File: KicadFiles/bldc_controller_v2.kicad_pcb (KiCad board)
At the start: 2 copper layers, 60 x 89 mm, 181 parts, among them J1 Conn_01x05_Male, J10 Conn_01x02_Female, J11 Conn_01x02_Female, J12 Conn_01x02_Female, J13 Conn_01x02_Female, J14 Conn_01x02_Female, J15 Conn_01x04_Male, J2 Conn_01x03_Male, J3 Conn_01x03_Male, J4 1935174, J5 Conn_01x02_Female, J9 Conn_01x02_Female, Q1 DMN65D8L-7, Q10 IRLB8721PBF, Q11 IRLB8721PBF, Q2 DMN65D8L-7, Q3 DMN65D8L-7, Q4 DMN65D8L-7, Q5 IRF4905, Q6 IRLB8721PBF, Q7 IRLB8721PBF, Q8 IRLB8721PBF, Q9 IRLB8721PBF, SW2 D6C40 F1 LFS, SW3 1301.9314, SW4 1301.9314, SW5 SW_Push_DPDT, U1 ATmega328P-PU, U2 uA7810, U3 LM7805_TO220, U4 MCP601-xP, U5 LM339, U6 IRS2004, U7 IRS2004, U8 IRS2004, U9 HCPL-181-00DE, Y1 9B-16.000MBBK-B

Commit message: Need to Update MCU Signals
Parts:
- C14, C22, C24, C28, C29, C32, D12, D13, D16, R10, R12, R13, R20, R22, R26, R33, R34, R35, R36, R37, R38, R39, R44, R45: moved to B.Cu
- moved D12 133.2 mm to (156.0, 140.2), turned to 270 degrees
- moved R10 124.8 mm to (163.2, 140.2), turned to 90 degrees
- moved D13 123.0 mm to (128.4, 144.0), turned to 270 degrees
- moved R20 122.7 mm to (140.5, 144.0), turned to 90 degrees
- moved R12 119.6 mm to (158.4, 140.2), turned to 270 degrees
- moved R5 114.8 mm to (70.2, 121.2)
- moved C14 114.2 mm to (160.8, 140.2), turned to 90 degrees
- moved D16 108.6 mm to (135.0, 104.5), turned to 180 degrees
- moved R26 108.3 mm to (142.8, 144.0), turned to 270 degrees
- moved R51 108.3 mm to (178.0, 124.4)
- moved C22 107.4 mm to (138.2, 144.0), turned to 90 degrees
- moved R49 103.6 mm to (167.8, 124.0)
- moved C24 101.9 mm to (133.0, 144.0), turned to 90 degrees
- moved R50 99.9 mm to (175.6, 116.8)
- moved R46 97.6 mm to (168.4, 119.0)
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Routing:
- net Net-(R37-Pad2): track 6.14 -> 14.6 mm, vias 0 -> 1
- net GNDD: track 0.00 -> 2.79 mm, vias 0 -> 1
- net /GATE_A_HI: track 0.00 -> 2.77 mm
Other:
- board size 60 x 89 mm -> 51.5 x 89 mm
- copper layers 2 -> 4

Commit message: Ready to Route
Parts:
- removed C13: 1uF, Capacitor_SMD:C_0805_2012Metric_Pad1.15x1.40mm_HandSolder
- removed D11: BAT54HT1G, Diode_SMD:D_SOD-323_HandSoldering
- removed D3: LTST-C171KRKT, LED_SMD:LED_0805_2012Metric_Pad1.15x1.40mm_HandSolder
- removed Q1, Q4: DMN65D8L-7, Package_TO_SOT_SMD:SOT-23
- removed R11: 100K, Resistor_SMD:R_0805_2012Metric_Pad1.15x1.40mm_HandSolder
- removed R18, R9: 10K, Resistor_SMD:R_0805_2012Metric_Pad1.15x1.40mm_HandSolder
- removed R2: 300, Resistor_SMD:R_0805_2012Metric_Pad1.15x1.40mm_HandSolder
- C15, C16, C23, C26, C36, C4, C6, C8, R15, R16, R17, R27, R28, R29, R30, R46, R47, R48, R52: moved to B.Cu
- moved J14 126.5 mm to (159.8, 135.2), turned to 90 degrees
- moved J11 124.3 mm to (156.0, 135.2), turned to 270 degrees
- moved J9 123.3 mm to (162.2, 128.0), turned to 270 degrees
- moved J10 123.0 mm to (147.2, 135.2), turned to 90 degrees
- moved J12 122.7 mm to (162.2, 131.5), turned to 270 degrees
- moved R3 121.8 mm to (156.0, 65.0)
- moved D6 116.1 mm to (152.0, 71.8), turned to 180 degrees
- moved J13 115.0 mm to (143.5, 135.2), turned to 270 degrees
- moved R6 112.0 mm to (156.0, 69.5)
- moved D1 110.6 mm to (152.0, 62.8), turned to 180 degrees
- moved D10 108.4 mm to (152.0, 74.0), turned to 180 degrees
- moved Q2 106.0 mm to (159.8, 71.0), turned to 180 degrees
- moved R7 103.8 mm to (156.0, 74.0)
- moved D7 103.1 mm to (152.0, 67.2), turned to 180 degrees
- moved C36 102.0 mm to (143.1, 128.0), turned to 90 degrees
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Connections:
- U1 pad 11: /nESTOP -> /MCU_C_EN
- U1 pad 12: /BEMF_A -> /MCU_C_SIG
- U1 pad 13: /BEMF_C -> /MCU_B_EN
- U1 pad 14: /BEMF_B -> /MCU_A_EN
- U1 pad 15: /MCU_C_SIG -> /MCU_A_SIG
- U1 pad 17: /MCU_A_SIG -> /EFUSE_EN
- U1 pad 18: /MCU_C_EN -> /AUX_OUT
- U1 pad 19: /MCU_B_EN -> /nESTOP
- U1 pad 23: /MCU_A_EN -> /ANALOG_IN
- U1 pad 24: /EFUSE_EN -> /AUX_IN
- U1 pad 25: /ANALOG_IN -> /I_SENSE
- U1 pad 26: /I_SENSE -> /BEMF_A
- U1 pad 4: /nI_TRIG -> /BEMF_C
- U1 pad 5: /AUX_IN -> /nI_TRIG
- U1 pad 6: /AUX_OUT -> /BEMF_B
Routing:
- net /EFUSE_GATE: track 0.00 -> 6.73 mm
- net /V_MOTOR: track 0.00 -> 4.85 mm
- net GNDD: track 2.79 -> 0.15 mm, vias 1 -> 0

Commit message: Began Routing
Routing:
- added copper zone on B.Cu, net +12V
- added copper zone on F.Cu, net +12V
- added copper zone on B.Cu, net +BATT
- added copper zone on F.Cu, net +BATT
- added copper zone on B.Cu, net /I_RAW
- added copper zone on B.Cu, net /V_MOTOR
- added copper zone on F.Cu, net /V_MOTOR
- added copper zone on B.Cu, net Net-(F1-Pad1)
- added copper zone on F.Cu, net Net-(F1-Pad1)
- added copper zone on F.Cu, net VBUS
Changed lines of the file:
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@@
   )
   (setup
-    (last_trace_width 0.762)
+    (last_trace_width 1.905)
     (user_trace_width 0.254)
     (user_trace_width 0.508)
     (user_trace_width 0.762)
     (user_trace_width 1.27)
+    (user_trace_width 1.905)
     (trace_clearance 0.2)
     (zone_clearance 0.508)
-    (zone_45_only no)
+    (zone_45_only yes)
     (trace_min 0.2)
     (via_size 0.8)
@@
   (segment (start 138.79 84.75) (end 138.75 84.79) (width 0.762) (layer In1.Cu) (net 67))
   (segment (start 146 84.75) (end 138.79 84.75) (width 0.762) (layer In1.Cu) (net 67))
+  (zone (net 2) (net_name +BATT) (layer F.Cu) (hatch edge 0.508)
+    (connect_pads (clearance 0.508))
+    (min_thickness 0.254)
+    (fill yes (arc_segments 32) (thermal_gap 0.508) (thermal_bridge_width 0.508))
+    (polygon
+      (pts
+        (xy 113.25 71) (xy 121.75 71) (xy 121.75 61.25) (xy 115.5 61.25) (xy 113.25 63.5)
+      )
+    )
+  )
+  (zone (net 2) (net_name +BATT) (layer B.Cu) (hatch edge 0.508)
+    (connect_pads (clearance 0.508))
+    (min_thickness 0.254)
+    (fill yes (arc_segments 32) (thermal_gap 0.508) (thermal_bridge_width 0.508))
+    (polygon
+      (pts
+        (xy 113.25 71) (xy 121.75 71) (xy 121.75 61.25) (xy 115.5 61.25) (xy 113.25 63.5)
+      )
+    )
+  )
+  (zone (net 32) (net_name "Net-(F1-Pad1)") (layer B.Cu) (hatch edge 0.508)
+    (connect_pads (clearance 0.508))
+    (min_thickness 0.254)
+    (fill yes (arc_segments 32) (thermal_gap 0.508) (thermal_bridge_width 0.508))
+    (polygon
+      (pts
+        (xy 122.75 71) (xy 128 71) (xy 128 61.25) (xy 122.75 61.25)
+      )
+    )
+  )
+  (zone (net 32) (net_name "Net-(F1-Pad1)") (layer F.Cu) (hatch edge 0.508)
+    (connect_pads (clearance 0.508))
+    (min_thickness 0.254)
+    (fill yes (arc_segments 32) (thermal_gap 0.508) (thermal_bridge_width 0.508))
+    (polygon
+      (pts
+        (xy 122.75 71) (xy 128 71) (xy 128 61.25) (xy 122.75 61.25)
+      )
+    )
+  )
+  (zone (net 7) (net_name +12V) (layer F.Cu) (hatch edge 0.508)
+    (connect_pads (clearance 0.508))
+    (min_thickness 0.254)
+    (fill yes (arc_segments 32) (thermal_gap 0.508) (thermal_bridge_width 0.508))
+    (polygon
+      (pts
+        (xy 130 61.25) (xy 130 71) (xy 136 71) (xy 136 61.25)
+      )
+    )
+  )
+  (zone (net 7) (net_name +12V) (layer B.Cu) (hatch edge 0.508)
+    (connect_pads (clearance 0.508))
+    (min_thickness 0.254)
+    (fill yes (arc_segments 32) (thermal_gap 0.508) (thermal_bridge_width 0.508))
+    (polygon
+      (pts
+        (xy 130 61.25) (xy 130 71) (xy 136 71) (xy 136 61.25)
+      )
+    )
+  )
+  (zone (net 12) (net_name /V_MOTOR) (layer F.Cu) (hatch edge 0.508)
+    (connect_pads (clearance 0.508))
+    (min_thickness 0.254)
+    (fill yes (arc_segments 32) (thermal_gap 0.508) (thermal_bridge_width 0.508))
+    (polygon
+      (pts
+        (xy 136.5 71) (xy 136.5 61.25) (xy 142 61.25) (xy 142 71)
+      )
+    )
+  )
+  (zone (net 12) (net_name /V_MOTOR) (layer B.Cu) (hatch edge 0.508)
+    (connect_pads (clearance 0.508))
+    (min_thickness 0.254)
+    (fill yes (arc_segments 32) (thermal_gap 0.508) (thermal_bridge_width 0.508))
+    (polygon
+      (pts
+        (xy 136.5 71) (xy 136.5 61.25) (xy 142 61.25) (xy 142 71)
+      )
+    )
+  )
+  (zone (net 3) (net_name VBUS) (layer F.Cu) (hatch edge 0.508)
+    (connect_pads (clearance 0.508))
+    (min_thickness 0.254)
+    (fill yes (arc_segments 32) (thermal_gap 0.508) (thermal_bridge_width 0.508))
+    (polygon
+      (pts
+        (xy 142.5 68) (xy 142.5 71.75) (xy 140 71.75) (xy 140 110.25) (xy 149.25 110.25)
+        (xy 149.25 61.25) (xy 142.5 61.25) (xy 142.5 71.75) (xy 142.5 68.25)
+      )
+    )
+  )
+  (zone (net 45) (net_name /I_RAW) (layer B.Cu) (hatch edge 0.508)
+    (connect_pads (clearance 0.508))
+    (min_thickness 0.254)
+    (fill yes (arc_segments 32) (thermal_gap 0.508) (thermal_bridge_width 0.508))
+    (polygon
+      (pts
+        (xy 135.75 75) (xy 135.75 79.5) (xy 140 79.5) (xy 140 110.25) (xy 147 110.25)
+        (xy 147 103.75) (xy 157 103.75) (xy 157 97.75) (xy 147 97.75) (xy 147 92.5)
+        (xy 157 92.5) (xy 157 86.5) (xy 147 86.5) (xy 147 81.25) (xy 157 81.25)
+        (xy 157 71.5) (xy 135.75 71.5)
+      )
+    )
+  )
 )

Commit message: Finished Planes
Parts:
- J10, J11, J12, J13, J14, J5, J9: footprint Connector_PinHeader_2.54mm:PinHeader_1x02_P2.54mm_Vertical -> Connector_PinSocket_2.54mm:PinSocket_1x02_P2.54mm_Vertical
- TP18, TP2, TP34, TP4: footprint TestPoint:TestPoint_THTPad_1.0x1.0mm_Drill0.5mm -> TestPoint:TestPoint_Keystone_5000-5004_Miniature
- moved R27 7.84 mm to (147.0, 110.2), turned to 0 degrees
- moved C26 4.91 mm to (147.0, 112.2), turned to 180 degrees
- moved R51 3.50 mm to (163.0, 123.2)
- moved R49 3.00 mm to (159.8, 123.2)
- moved Q2 1.52 mm to (160.0, 69.5)
- moved Q3 1.52 mm to (160.0, 73.2)
- moved R50 0.25 mm to (156.5, 123.2)
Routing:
- net /PHASE_A: track 0.00 -> 54.9 mm, vias 0 -> 9
- net GNDD: track 0.15 -> 51.6 mm, vias 0 -> 5
- net /PHASE_B: track 0.00 -> 43.3 mm, vias 0 -> 9
- net /PHASE_C: track 0.00 -> 27.5 mm, vias 0 -> 9
- net +10V: track 0.00 -> 22.0 mm
- net Net-(R34-Pad2): track 0.00 -> 20.2 mm, vias 0 -> 1
- net Net-(R36-Pad2): track 0.00 -> 20.1 mm, vias 0 -> 1
- net Net-(R35-Pad2): track 0.00 -> 17.1 mm, vias 0 -> 1
- net Net-(R38-Pad2): track 0.00 -> 14.8 mm, vias 0 -> 1
- net Net-(R39-Pad2): track 0.00 -> 14.2 mm, vias 0 -> 1
- net GNDPWR: track 0.00 -> 14.0 mm
- net /EFUSE_EN: track 0.00 -> 13.1 mm
- net VBUS: track 0.00 -> 9.17 mm
- net +5V: track 0.00 -> 8.77 mm
- net Net-(R14-Pad1): track 0.00 -> 7.31 mm
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- added copper zone on In1.Cu, net +10V
- added copper zone on In1.Cu, net +12V
- added copper zone on In1.Cu, net +5V
- added copper zone on B.Cu, net /PHASE_A
- added copper zone on F.Cu, net /PHASE_A
- added copper zone on B.Cu, net /PHASE_B
- added copper zone on F.Cu, net /PHASE_B
- added copper zone on B.Cu, net /PHASE_C
- added copper zone on F.Cu, net /PHASE_C
- added copper zone on Gnd.Cu, net GNDD
- added copper zone on Gnd.Cu, net GNDPWR

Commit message: Finished First Pass of Routing
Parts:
- moved C14 14.5 mm to (146.3, 139.9)
- moved D12 14.5 mm to (141.5, 139.9)
- moved R12 14.5 mm to (143.9, 139.9)
- moved R10 12.0 mm to (151.2, 139.9)
- moved R49 3.25 mm to (163.0, 123.3)
- moved R51 3.25 mm to (159.8, 123.2)
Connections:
- J15 pad 2: /I2C_SCL -> /I2C_SDA
- J15 pad 3: /I2C_SDA -> /I2C_SCL
- SW2 pad 1: Net-(R10-Pad1) -> /nESTOP
- SW2 pad 2: /nESTOP -> Net-(R10-Pad1)
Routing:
- net +5V: track 8.77 -> 90.8 mm, vias 0 -> 5
- net /EFUSE_EN: track 13.1 -> 89.3 mm, vias 0 -> 3
- net /AUX_OUT: track 0.00 -> 73.1 mm, vias 0 -> 2
- net /nESTOP: track 0.00 -> 59.9 mm
- net /AUX_IN: track 0.00 -> 49.2 mm, vias 0 -> 1
- net +10V: track 22.0 -> 53.2 mm, vias 0 -> 1
- net /BEMF_A: track 0.00 -> 25.3 mm
- net /BEMF_C: track 0.00 -> 21.4 mm
- net /nI_TRIG: track 0.00 -> 21.4 mm
- net /B_FILT: track 0.00 -> 20.6 mm
- net /BEMF_B: track 0.00 -> 18.6 mm
- net /MCU_A_SIG: track 0.00 -> 18.3 mm
- net +12V: track 3.48 -> 21.2 mm, vias 1 -> 2
- net GNDD: track 51.6 -> 68.3 mm, vias 5 -> 9
- net /MCU_B_SIG: track 0.00 -> 15.5 mm
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- added copper zone on F.Cu, net /NEUTRAL

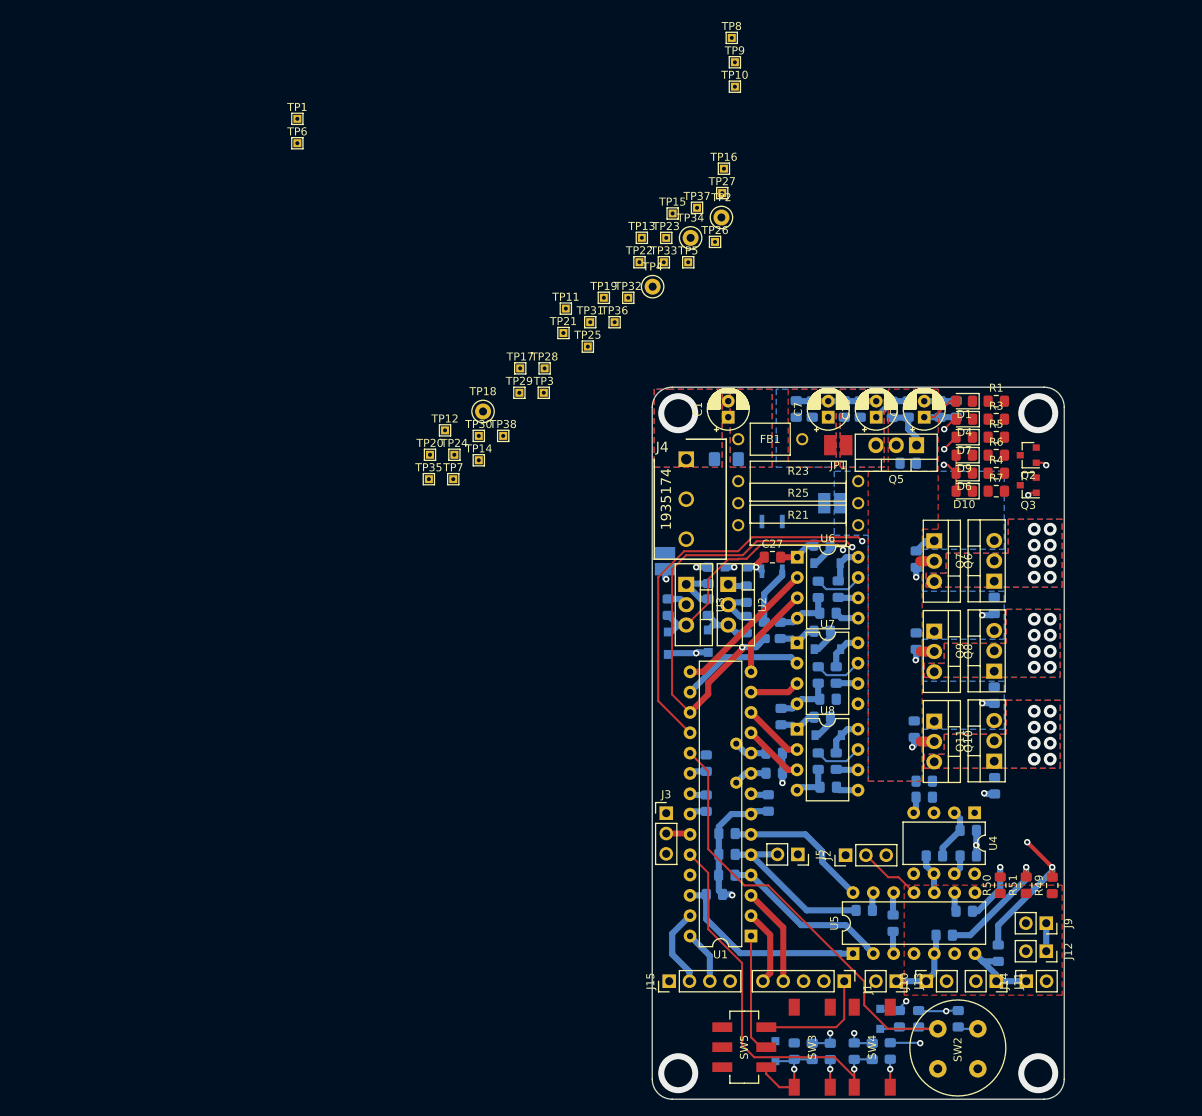
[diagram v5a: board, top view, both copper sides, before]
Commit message: Connected Test Points
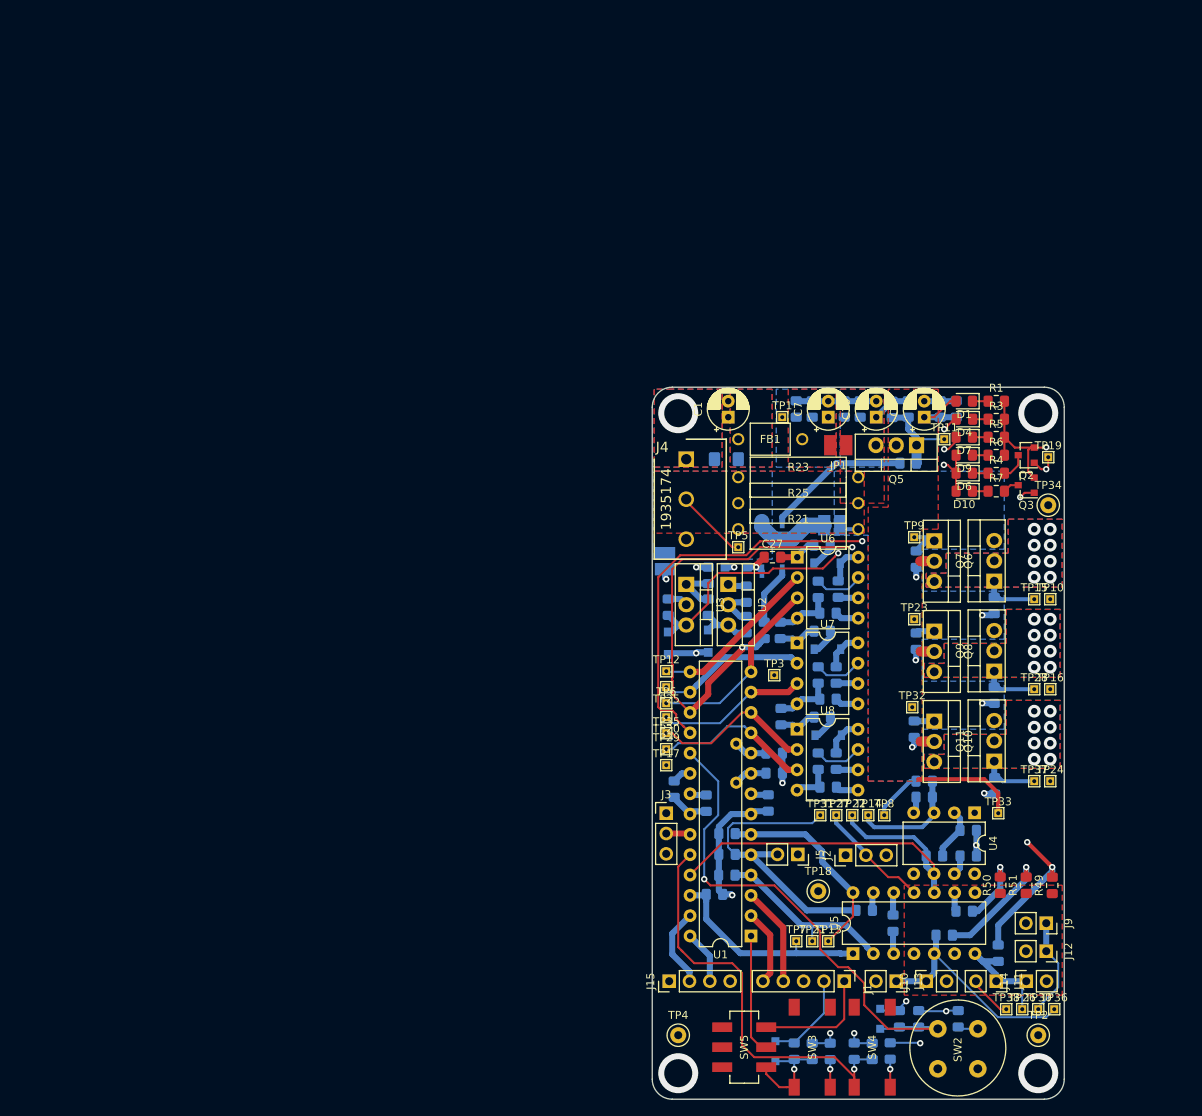
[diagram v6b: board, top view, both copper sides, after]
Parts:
- moved TP2 109.6 mm to (161.2, 142.0)
- moved TP26 103.3 mm to (159.2, 138.8)
- moved TP36 102.0 mm to (163.2, 138.8)
- moved TP30 100.1 mm to (161.2, 138.8)
- moved TP8 99.0 mm to (142.0, 114.5)
- moved TP38 95.3 mm to (157.2, 138.8)
- moved TP4 93.6 mm to (116.2, 142.0)
- moved TP13 91.0 mm to (135.0, 130.2)
- moved TP24 84.9 mm to (162.8, 110.2)
- moved TP6 83.8 mm to (114.8, 100.5)
- moved TP37 83.1 mm to (160.8, 110.2)
- moved TP21 82.1 mm to (133.0, 130.2)
- moved TP33 80.6 mm to (156.2, 114.2)
- moved TP27 79.1 mm to (136.0, 114.5)
- moved TP16 76.8 mm to (162.8, 98.8)
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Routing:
- net GNDD: track 68.3 -> 162.5 mm, vias 9 -> 10
- net /I_SENSE: track 5.00 -> 51.8 mm
- net /C_FILT: track 10.0 -> 28.7 mm
- net Net-(R24-Pad2): track 0.00 -> 18.1 mm
- net /nI_TRIG: track 21.4 -> 37.2 mm
- net /I_FILT: track 0.00 -> 14.3 mm
- net /MCU_C_SIG: track 7.67 -> 21.4 mm
- net VBUS: track 14.0 -> 27.2 mm
- net /MCU_B_EN: track 6.20 -> 18.7 mm
- net /MCU_A_EN: track 11.6 -> 23.9 mm
- net /MCU_C_EN: track 7.67 -> 19.8 mm
- net +5V: track 90.8 -> 102.6 mm
- net GNDPWR: track 14.0 -> 23.9 mm
- net /V_MOTOR: track 4.85 -> 14.0 mm
- net /GATE_C_LO: track 0.00 -> 8.96 mm
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- added copper zone on B.Cu, net GNDPWR

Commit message: Fixed Unconnected Nets
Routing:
- net +BATT: track 0.00 -> 3.50 mm
- net /GATE_C_HI: track 2.51 -> 4.34 mm
- net /GATE_B_HI: track 2.34 -> 4.17 mm
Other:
- rule trace_min: 0.2 -> 0.25
- rule via_min_size: 0.4 -> 0.45
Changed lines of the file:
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@@
     (thickness 1.6)
     (drawings 8)
-    (tracks 708)
+    (tracks 714)
     (zones 0)
     (modules 172)
@@
   )
   (setup
-    (last_trace_width 0.254)
+    (last_trace_width 0.508)
     (user_trace_width 0.254)
     (user_trace_width 0.508)
@@
     (zone_clearance 0.508)
     (zone_45_only yes)
-    (trace_min 0.2)
+    (trace_min 0.25)
     (via_size 0.8)
     (via_drill 0.4)
-    (via_min_size 0.4)
+    (via_min_size 0.45)
     (via_min_drill 0.3)
     (uvia_size 0.3)
@@
     (aux_axis_origin 0 0)
     (grid_origin 113 61)
-    (visible_elements 7FFFB7FF)
+    (visible_elements 7FFFBFFF)
     (pcbplotparams
       (layerselection 0x010fc_ffffffff)
@@
   (segment (start 134.5 78.25) (end 132.25 78.25) (width 1.905) (layer B.Cu) (net 1))
   (segment (start 132.25 78.25) (end 130.5 80) (width 1.905) (layer B.Cu) (net 1))
+  (segment (start 122.5 64.75) (end 120.75 64.75) (width 0.508) (layer F.Cu) (net 2))
+  (segment (start 122.5 64.75) (end 120.75 64.75) (width 0.508) (layer B.Cu) (net 2))
   (segment (start 147 64.75) (end 151 64.75) (width 0.762) (layer B.Cu) (net 3))
   (segment (start 148.25 82.75) (end 146.5 82.75) (width 1.27) (layer F.Cu) (net 3))
@@
   (segment (start 146.225 91.5) (end 146 91.725) (width 0.762) (layer B.Cu) (net 52))
   (segment (start 148.25 91.5) (end 146.225 91.5) (width 0.762) (layer B.Cu) (net 52))
+  (segment (start 145.75 91.475) (end 146 91.725) (width 0.508) (layer B.Cu) (net 52))
+  (segment (start 145.75 90) (end 145.75 91.475) (width 0.508) (layer B.Cu) (net 52))
   (segment (start 155.75 96.5) (end 155.75 98.475) (width 0.762) (layer B.Cu) (net 53))
   (segment (start 155.75 97.9605) (end 155.75 96.5) (width 0.508) (layer B.Cu) (net 53))
@@
   (segment (start 145.775 102.75) (end 145.75 102.725) (width 0.762) (layer B.Cu) (net 54))
   (segment (start 148.25 102.75) (end 145.775 102.75) (width 0.762) (layer B.Cu) (net 54))
+  (segment (start 145.5 102.475) (end 145.75 102.725) (width 0.508) (layer B.Cu) (net 54))
+  (segment (start 145.5 101) (end 145.5 102.475) (width 0.508) (layer B.Cu) (net 54))
   (segment (start 155.75 109.75) (end 155.8 109.8) (width 0.762) (layer B.Cu) (net 55))
   (segment (start 155.75 107.75) (end 155.75 109.75) (width 0.762) (layer B.Cu) (net 55))
